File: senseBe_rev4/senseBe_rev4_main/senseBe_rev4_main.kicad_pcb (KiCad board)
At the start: 2 copper layers, 60 x 38 mm, 57 parts, among them J1 PJ-611-5A_AudioJack, P1 CONN_02X05, Q1 SI2302, Q2 SI2302, Q3 SI2302, Q4 SI2302, Q5 TSM2301, Q6 SI2302, Q7 SI2302, SW1 SW_Push_SPDT, SW2 SW_Push_Dual, U1 MDBT42Q, U2 TSSP4056, U3 AP3405, Y1 Crystal

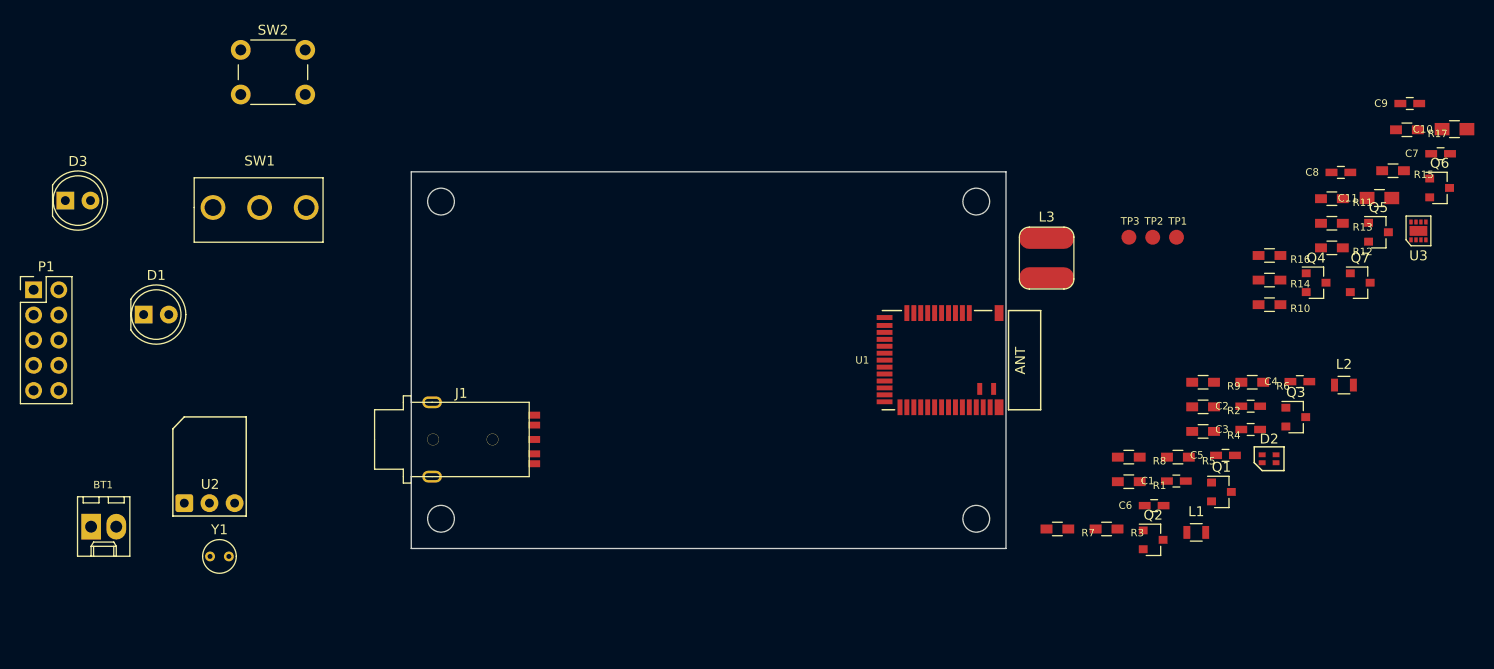
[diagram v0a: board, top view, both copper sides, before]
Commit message: senseBe_rev4 and sense_rev5 schematic and PCB placement done.
PCB placement for all major components that affect the mechanical enclosure design is done, and locked.
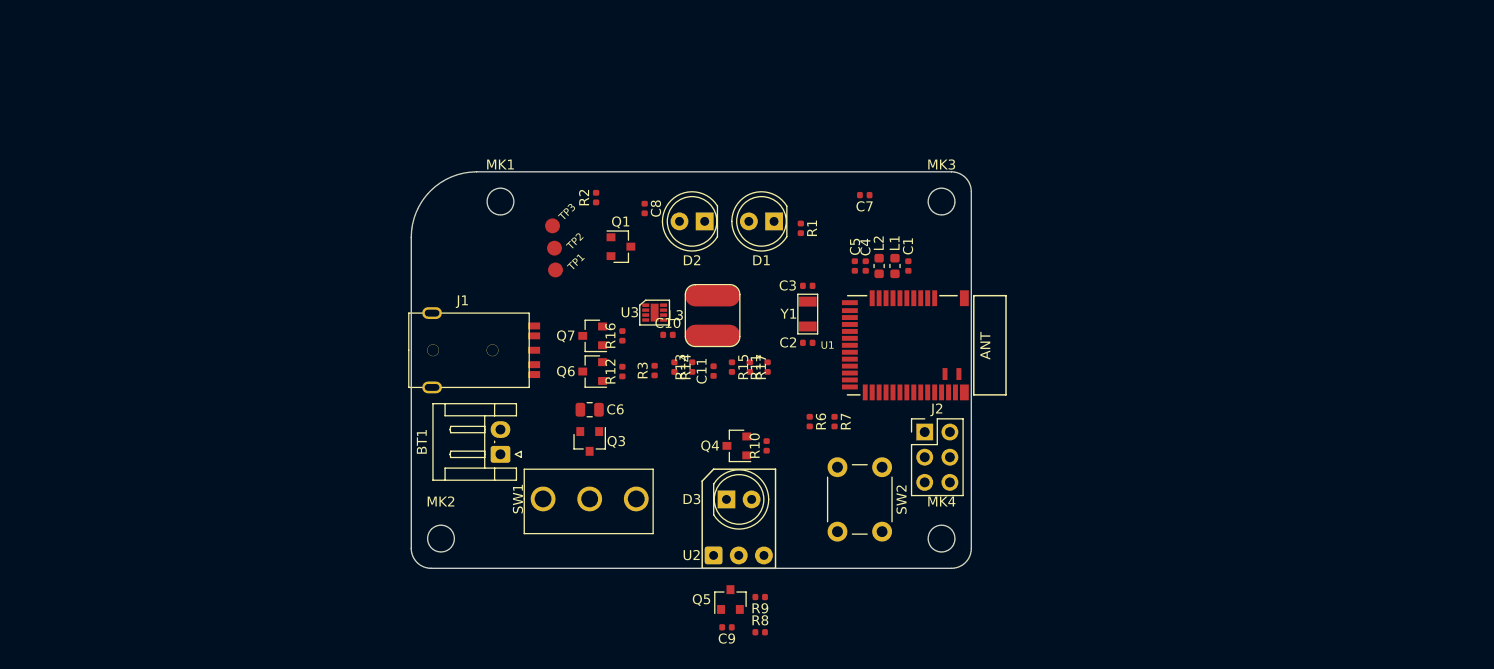
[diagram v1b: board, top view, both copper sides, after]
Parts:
- removed P1: CONN_02X05, Connector_PinHeader_2.54mm:PinHeader_2x05_P2.54mm_Vertical
- removed Q2: SI2302, sense:SOT-23
- removed R4: 24, sense:R_0603_HandSoldering
- removed R5: 470k, sense:R_0603_HandSoldering
- added J2: Conn_01x06, Connector_PinHeader_2.54mm:PinHeader_2x03_P2.54mm_Vertical, F.Cu at (61.8, 36.2)
- BT1: footprint sense:Molex_KK-6410-02_02x2.54mm_Straight -> Connector_JST:JST_EH_S2B-EH_1x02_P2.50mm_Horizontal
- C1, C2, C3, C4, C5, C7, C8: footprint sense:C_0603_HandSoldering -> Capacitor_SMD:C_0402_1005Metric
- C10, C11: footprint sense:C_0805_HandSoldering -> Capacitor_SMD:C_0402_1005Metric
- C6: value 100nF -> 10Uf; footprint sense:C_0603_HandSoldering -> Capacitor_SMD:C_0805_2012Metric
- C9: value 10uF -> 100nF; footprint sense:C_0603_HandSoldering -> Capacitor_SMD:C_0402_1005Metric
- D2: value 18-225/R6G6C-A01/3T -> LED; footprint sense:18-225_R6G6C-A01_3T -> LED_THT:LED_D5.0mm
- L1, L2: footprint sense:L_0805 -> Inductor_SMD:L_0603_1608Metric
- MK1, MK2, MK3, MK4: footprint MountingHole:MountingHole_2.7mm_M2.5 -> sense:MountingHole_2.7mm_M2.5
- Q1: value SI2302 -> 2N7002; footprint sense:SOT-23 -> Package_TO_SOT_SMD:SOT-23
- Q3: value SI2302 -> TSM2301
- Q5: value TSM2301 -> SI2302
- R1, R10, R11, R12, R13, R14, R15, R16, R17, R2, R3, R6, R7, R8, R9: footprint sense:R_0603_HandSoldering -> Resistor_SMD:R_0402_1005Metric
- SW2: value SW_Push_Dual -> SW_SPST
- Y1: footprint sense:Crystal_C38-LF_d3.0mm_l8.0mm_Vertical -> sense:Q13FC1350000400_SMD Crystals 32.768KHz
- moved Q6 87.4 mm to (28.3, 30.1), turned to 180 degrees
- moved C9 86.8 mm to (41.9, 56.0), turned to 180 degrees
- moved C10 82.0 mm to (35.9, 26.4)
- moved Q7 77.6 mm to (28.3, 26.6), turned to 180 degrees
- moved U3 77.5 mm to (34.5, 24.2), turned to 270 degrees
- moved SW2 77.2 mm to (57.5, 39.8), turned to 270 degrees
- moved Q5 75.1 mm to (42.2, 53.1), turned to 90 degrees
- moved D3 73.2 mm to (41.8, 43.0)
- moved R12 72.7 mm to (31.3, 30.1), turned to 90 degrees
- moved Q3 71.3 mm to (28.0, 37.2), turned to 270 degrees
- moved R17 70.5 mm to (44.1, 29.7), turned to 270 degrees
- moved C8 70.3 mm to (33.5, 13.7), turned to 270 degrees
- moved R15 69.6 mm to (42.4, 29.7), turned to 270 degrees
- moved C11 69.4 mm to (40.5, 30.1), turned to 90 degrees
- moved R13 66.1 mm to (38.4, 29.7), turned to 90 degrees
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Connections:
- C7 pad 1: GND -> /BUTTON
- C7 pad 2: /Sheet5C63BFE7/BUTTON -> GND
- D2 pad 1: VDD -> Net-(D2-Pad1)
- D2 pad 2: Net-(D2-Pad2) -> VDD
- J1 pad 1: /Sheet5C63BFE7/TRIGGER -> /TRIGGER
- J1 pad 2: /Sheet5C63BFE7/FOCUS -> /FOCUS
- J1 pad 3: /Sheet5C63BFE7/CAM_JACK -> /CAM_JACK
- J1 pad 5: /Sheet5C63BFE7/FOCUS -> /FOCUS
- Q3 pad 1: /RX_EN -> GND
- Q3 pad 2: GND -> VDD
- Q5 pad 1: GND -> /RX_EN
- Q5 pad 2: VDD -> GND
- R3 pad 1: Net-(Q2-Pad3) -> Net-(D2-Pad1)
- R3 pad 2: Net-(D2-Pad2) -> Net-(Q1-Pad3)
- R8 pad 1: Net-(Q3-Pad3) -> Net-(Q5-Pad3)
- SW1 pad 3: Net-(Q5-Pad3) -> Net-(Q3-Pad3)
- SW2 pad 2: GND -> /BUTTON
- U1 pad 17: /VLED -> /LED_RED
- U1 pad 18: /PWR1 -> /VLED
- U1 pad 2: Net-(U1-Pad2) -> /LIGHT_SENSE_EN
- U1 pad 20: /RX_EN -> /PWR1
- U1 pad 21: /RX_OUT -> /IR_LED_EN
- U1 pad 22: /LED_RED -> /RX_EN
- U1 pad 23: /LED_GREEN -> /RX_OUT
- U1 pad 3: Net-(U1-Pad3) -> /REG_EN
- U1 pad 32: /BUTTON -> Net-(U1-Pad32)
- U1 pad 4: /REG_EN -> /BUTTON
- U1 pad 6: /LIGHT_SENSE_EN -> Net-(U1-Pad6)
- U1 pad 7: /IR_LED_EN -> Net-(U1-Pad7)
- U2 pad 2: Net-(Q3-Pad3) -> Net-(Q5-Pad3)
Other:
- board size 60 x 38 mm -> 56.5 x 40 mm
- board text added: "www.appiko.org"

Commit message: senseBe_rev4 PCB layout done.
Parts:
- removed Q3: TSM2301, sense:SOT-23
- added G***: LOGO, sense:OSHW1, B.Cu at (38.2, 30.0)
- added G***: Appiko_Logo_2, sense:Appiko_Logo_2, F.Cu at (20.9, 18.0)
- added G***: Appiko_LOGO_img, sense:Appiko_LOGO_img, B.Cu at (28.2, 18.1)
- added Q2: Q_PMOS_GDS, sense:SOT-23, F.Cu at (25.5, 37.2)
- C10: value 22u -> 22uF; footprint Capacitor_SMD:C_0402_1005Metric -> Capacitor_SMD:C_0603_1608Metric
- C11: value 8p -> 8pF
- C5, C7, C9: value 100nF -> 0.1uF
- C6: value 10Uf -> 10uF
- C8: value 10u -> 22uF; footprint Capacitor_SMD:C_0402_1005Metric -> Capacitor_SMD:C_0603_1608Metric
- J2: value Conn_01x06 -> Conn_02x03_Odd_Even
- L3: value 22u -> 22uH
- Q1: value 2N7002 -> SI2302; footprint Package_TO_SOT_SMD:SOT-23 -> sense:SOT-23
- R3: value 33 -> 33E
- moved TP1 37.6 mm to (58.1, 36.8)
- moved TP2 36.8 mm to (55.9, 36.8)
- moved C7 32.8 mm to (50.2, 44.6), turned to 270 degrees
- moved R2 28.9 mm to (57.5, 13.2)
- moved C8 25.4 mm to (45.9, 35.9)
- moved Q1 24.0 mm to (54.8, 13.2), turned to 180 degrees
- moved R3 23.8 mm to (51.4, 13.2), turned to 270 degrees
- moved R11 16.9 mm to (30.0, 24.2), turned to 180 degrees
- moved R9 14.4 mm to (37.0, 41.0)
- moved C9 13.1 mm to (48.5, 44.6), turned to 90 degrees
- moved R8 12.9 mm to (37.0, 46.5), turned to 180 degrees
- moved L3 12.1 mm to (33.5, 34.5), turned to 90 degrees
- moved R17 12.0 mm to (33.5, 24.2), turned to 0 degrees
- moved Q6 11.0 mm to (39.2, 31.1)
- moved Q7 11.0 mm to (39.2, 27.5)
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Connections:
- J2 pad 2: /SWDCLK -> /RX
- J2 pad 3: /TX -> /SWDCLK
- J2 pad 4: /RX -> VDD
- J2 pad 5: VDD -> /TX
- U1 pad 17: /LED_RED -> /REG_EN
- U1 pad 2: /LIGHT_SENSE_EN -> /LED_RED
- U1 pad 25: /RX_TX_S -> /TRIGGER
- U1 pad 28: /TRIGGER -> /RX_TX_S
- U1 pad 29: Net-(U1-Pad29) -> /BUTTON
- U1 pad 3: /REG_EN -> /LIGHT_SENSE_EN
- U1 pad 30: /GPIO2 -> Net-(U1-Pad30)
- U1 pad 31: /GPIO1 -> /GPIO2
- U1 pad 32: Net-(U1-Pad32) -> /GPIO1
- U1 pad 4: /BUTTON -> /LIGHT_SENSE
- U1 pad 5: /LIGHT_SENSE -> Net-(U1-Pad5)
- U3 pad 6: VDD -> Net-(U3-Pad6)
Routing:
- net VDD: track 0.00 -> 128.3 mm, vias 0 -> 4
- net GND: track 0.00 -> 78.5 mm, vias 0 -> 28
- net /FOCUS: track 0.00 -> 52.1 mm, vias 0 -> 2
- net /CAM_JACK: track 0.00 -> 46.9 mm, vias 0 -> 2
- net /TRIGGER: track 0.00 -> 46.8 mm, vias 0 -> 2
- net /VLED: track 0.00 -> 41.5 mm, vias 0 -> 2
- net /REG_EN: track 0.00 -> 30.9 mm, vias 0 -> 2
- net /RX_EN: track 0.00 -> 24.8 mm, vias 0 -> 2
- net /RX_OUT: track 0.00 -> 24.0 mm
- net /BUTTON: track 0.00 -> 21.9 mm, vias 0 -> 1
- net /LIGHT_SENSE: track 0.00 -> 21.7 mm
- net /LIGHT_SENSE_EN: track 0.00 -> 18.9 mm
- net /IR_LED_EN: track 0.00 -> 16.3 mm
- net /PWR1: track 0.00 -> 15.3 mm
- net /PWR2: track 0.00 -> 14.3 mm
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- added copper zone on B.Cu, net GND
- added copper zone on F.Cu, net GND
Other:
- board text added: "senseBe_rev4"

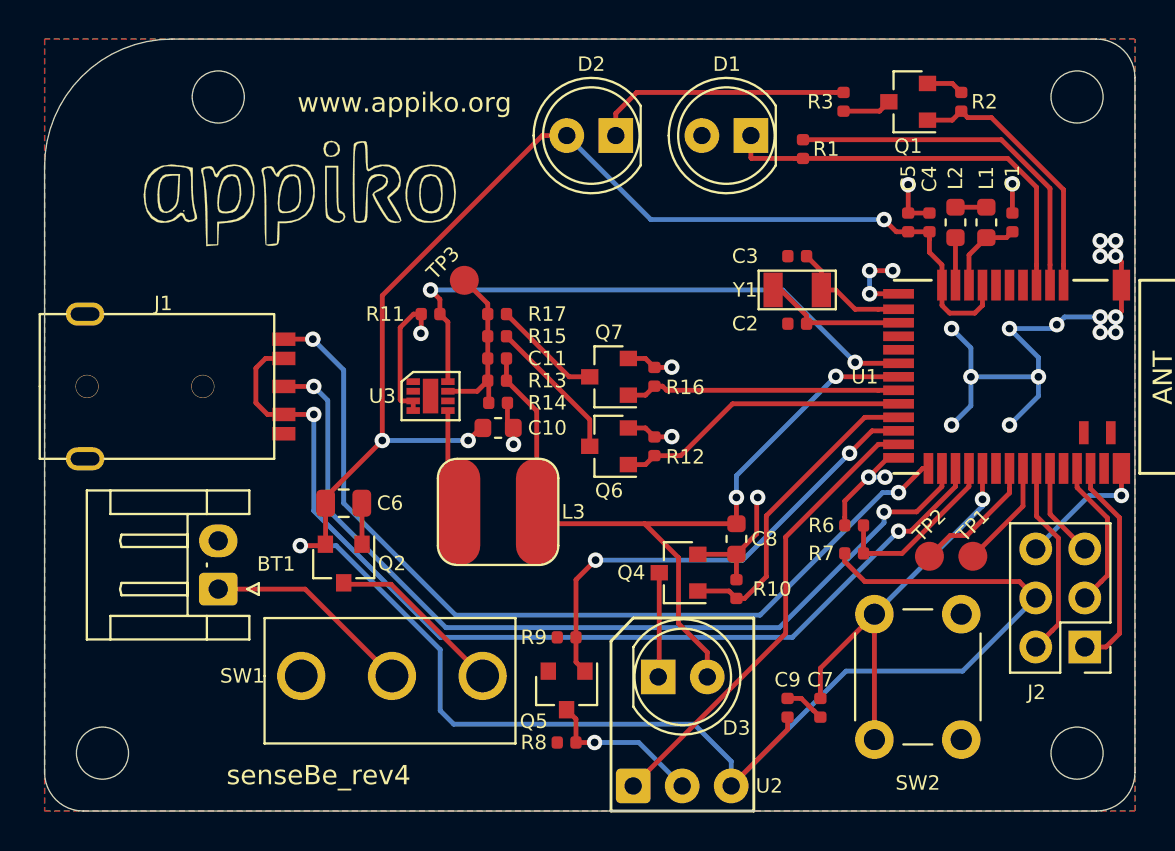
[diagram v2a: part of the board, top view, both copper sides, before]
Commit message: Add the RTC in the schematic and PCB
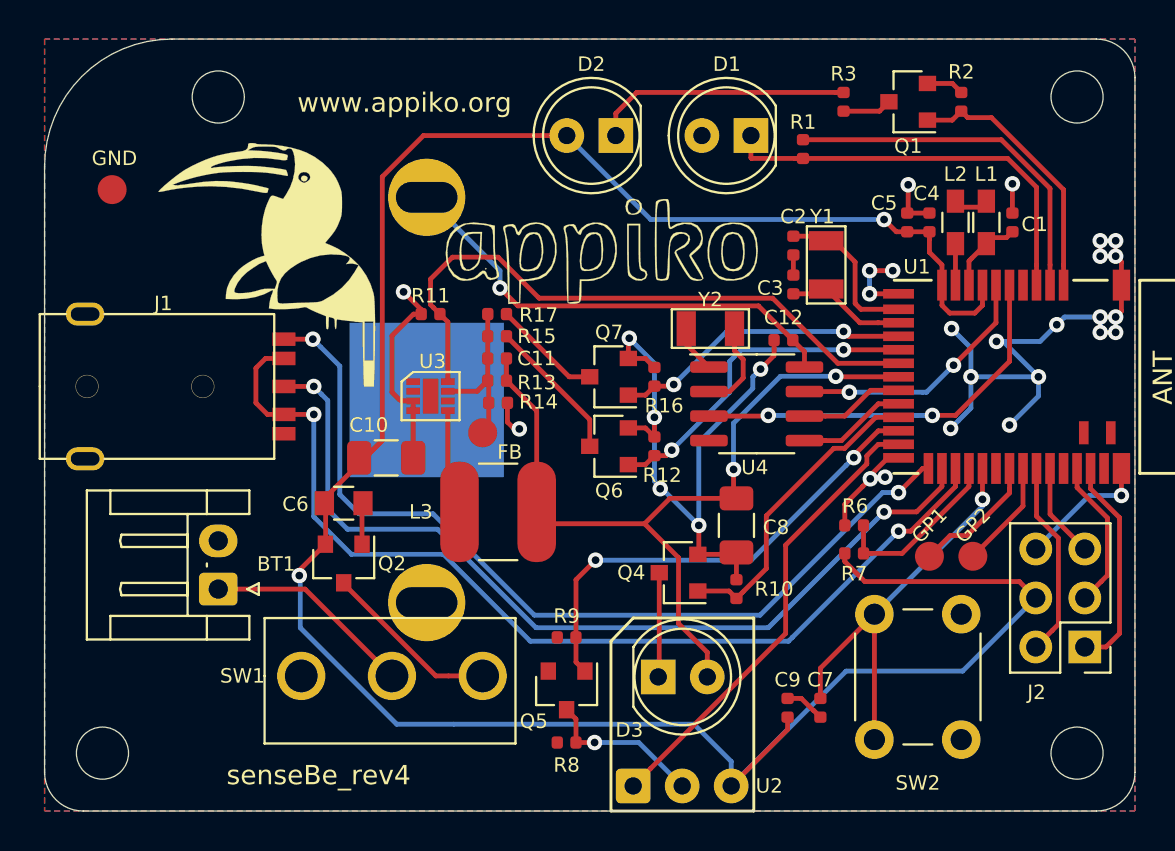
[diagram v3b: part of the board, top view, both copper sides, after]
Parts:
- removed the G*** at (38.2, 30.0)
- removed the G*** at (20.9, 18.0)
- removed the G*** at (28.2, 18.1)
- removed TP1, TP2: TestPoint, sense:Measurement_Point_Round-SMD-Pad_Small
- removed TP3: FB_TP, sense:Measurement_Point_Round-SMD-Pad_Small
- added BT2: CR2032 holder, sense_fp:BatteryHolder_Keystone_3009_1x2450, B.Cu at (29.8, 28.7)
- added C12: 0.1uF, sense_fp:C_0402_1005Metric, F.Cu at (48.3, 25.6)
- added FB: FB_TP, sense_fp:Measurement_Point_Round-SMD-Pad_Small, F.Cu at (32.7, 30.4)
- added G***: LOGO, sense_fp:OSHW1, B.Cu at (55.2, 18.7)
- added G***: Appiko_Logo_2, sense_fp:Appiko_Logo_2, F.Cu at (36.6, 21.0)
- added G***: Appiko_LOGO_img, sense_fp:Appiko_LOGO_img, F.Cu at (21.5, 21.7)
- added GND: TestPoint, sense_fp:Measurement_Point_Round-SMD-Pad_Small, F.Cu at (13.5, 17.8)
- added GP1: TestPoint, sense_fp:Measurement_Point_Round-SMD-Pad_Small, F.Cu at (55.9, 36.8)
- added GP2: TestPoint, sense_fp:Measurement_Point_Round-SMD-Pad_Small, F.Cu at (58.1, 36.8)
- added U4: PCF8563T, sense_fp:SOIC-8_3.9x4.9mm_P1.27mm, F.Cu at (46.9, 28.9)
- added Y2: Q13FC1350000400, sense_fp:Q13FC1350000400_SMD Crystals 32.768KHz, F.Cu at (44.5, 25.0)
- BT1: footprint Connector_JST:JST_EH_S2B-EH_1x02_P2.50mm_Horizontal -> sense_fp:JST_EH_S2B-EH_1x02_P2.50mm_Horizontal
- C1, C11, C2, C3, C4, C5, C7, C9: footprint Capacitor_SMD:C_0402_1005Metric -> sense_fp:C_0402_1005Metric
- C10, C8: footprint Capacitor_SMD:C_0603_1608Metric -> sense_fp:C_1206_3216Metric
- C6: footprint Capacitor_SMD:C_0805_2012Metric -> sense_fp:C_0805
- D1, D2, D3: footprint LED_THT:LED_D5.0mm -> sense_fp:LED_D5.0mm
- J1: footprint sense:PJ_611_5A_Audio Jack -> sense_fp:PJ_611_5A_Audio Jack
- J2: footprint Connector_PinHeader_2.54mm:PinHeader_2x03_P2.54mm_Vertical -> sense_fp:PinHeader_2x03_P2.54mm_Vertical
- L1, L2: footprint Inductor_SMD:L_0603_1608Metric -> sense_fp:L_0603_HandSoldering
- L3: footprint sense:22uH_SMD_5mm_Inductor -> sense_fp:L_5mm_SMD_copy
- MK1, MK2, MK3, MK4: footprint sense:MountingHole_2.7mm_M2.5 -> sense_fp:MountingHole_2.7mm_M2.5
- Q1, Q2, Q4, Q5, Q6, Q7: footprint sense:SOT-23 -> sense_fp:SOT-23
- R1, R10, R11, R12, R13, R14, R15, R16, R17, R2, R3, R6, R7, R8, R9: footprint Resistor_SMD:R_0402_1005Metric -> sense_fp:C_0402_1005Metric
- SW1: footprint sense:SlideSwitch_1P2T_Straight -> sense_fp:SlideSwitch_1P2T_Straight
- SW2: footprint sense:SW_PUSH_6mm -> sense_fp:SW_PUSH_6mm
- U1: footprint sense:mdbt42Q -> sense_fp:mdbt42Q
- U2: footprint sense:Vishay_MINIMOLD-3Pin -> sense_fp:Vishay_MINIMOLD-3Pin
- Y1: footprint sense:Q13FC1350000400_SMD Crystals 32.768KHz -> sense_fp:Q13FC1350000400_SMD Crystals 32.768KHz
- moved C10 6.00 mm to (27.7, 31.7)
- moved C2 2.04 mm to (48.8, 22.7), turned to 270 degrees
- moved Y1 1.98 mm to (50.5, 21.7), turned to 90 degrees
- moved C8 0.70 mm to (45.9, 35.2)
- moved C3 0.59 mm to (48.8, 20.7), turned to 90 degrees
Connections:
- U1 pad 15: Net-(U1-Pad15) -> /PWR2
- U1 pad 16: Net-(U1-Pad16) -> /PWR1
- U1 pad 19: /PWR2 -> /SCL
- U1 pad 20: /PWR1 -> /SDA
- U1 pad 6: Net-(U1-Pad6) -> /RTC_INT
- U1 pad 7: Net-(U1-Pad7) -> /RTC_CLK
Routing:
- net GND: track 78.5 -> 108.6 mm, vias 28 -> 30
- net Net-(BT2-Pad1): track 0.00 -> 24.2 mm, vias 0 -> 1
- net /RTC_INT: track 0.00 -> 20.7 mm, vias 0 -> 2
- net /RTC_CLK: track 0.00 -> 13.4 mm, vias 0 -> 2
- net /SDA: track 0.00 -> 5.66 mm
- net /SCL: track 0.00 -> 5.43 mm
- net Net-(U4-Pad2): track 0.00 -> 4.82 mm
- net Net-(U4-Pad1): track 0.00 -> 2.48 mm
- net /PWR1: track 15.3 -> 17.4 mm, vias 0 -> 2
- net /LFCLK_XL1: track 6.48 -> 8.28 mm
- net /REG_EN: track 30.9 -> 32.7 mm, vias 2 -> 0
- net /LFCLK_XL2: track 7.49 -> 6.28 mm
- net /PWR2: track 14.3 -> 15.5 mm, vias 0 -> 2
- net /VLED: track 41.5 -> 42.6 mm
- net Net-(C11-Pad2): track 9.17 -> 8.59 mm
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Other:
- net class Default: clearance 0.2 -> 0.15
- rule trace_clearance: 0.2 -> 0.15
